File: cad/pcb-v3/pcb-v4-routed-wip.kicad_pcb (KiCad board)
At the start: 4 copper layers, 19.3 x 19.3 mm, 50 parts

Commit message: Zone fill landed; BOM gains U5 + the three 0201s. 4 blockers left.
The KiCad fill worked -- blocker 18 (zones carry no fill) is cleared and
preflight now sees the In2.Cu plane.

NOTE THE FILE FORMAT CHANGED UNDER US. KiCad 20260206 rewrote the board from
(net <n>) + (net_name "X") to a single (net "X"): 165 numbered declarations
and 980 bare ordinals became 0, replaced by 1100 name strings. preflight
survives it (check 4 still matches 134 pins) but any parser in this repo keyed
on (net <digits>) will silently read ZERO nets on a board saved by this KiCad.
Checked before trusting the output rather than after.

BOM: U5 C6989585 (consigned from Digi-Key, JLC stock 0/min 5), R8 C274872,
R9 C273271, C14 C76939 -- the 25 V cap, not the 10 V one, because DC bias
already cost C1/C2 once. Blocker 21 cleared.

Remaining: 4 clearance violations, 16 true open pads, 11 router DRC
violations, GND not fully connected.
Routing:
- net GND: track 0.00 -> 19.9 mm, vias 0 -> 16
- added copper zone on In2.Cu, net GND

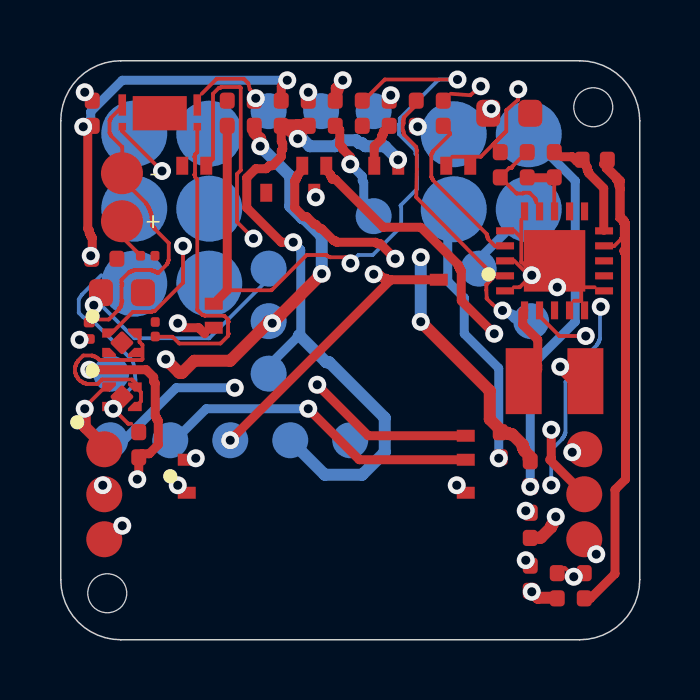
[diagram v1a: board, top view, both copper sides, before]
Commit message: Routing: 3 opens left, and none of them are the PCM's
Placing the 0201s nearest-to-U5 was the wrong objective and it was mine. It
walked R8/R9/C14 up the LEFT STRIP -- 2.72 mm wide, already carrying U3, U4
(X2SON-4, pads 0.34-0.40 apart) and C5 -- and the opens came back clustered on
exactly those parts. They are now scored by ELBOW ROOM within a bounded radius
of U5 instead.

  before: 10-12 open pads pre-stitch, 4 NO PATH after
  after :  4 open pads pre-stitch, 3 NO PATH after

PCM_VDD R8.2 and BL_RETURN R6.1 are gone -- the parts the PCM added now route.

Bounded, not free: pure elbow room threw R9 21.5 mm into the far corner, and
R9 is the V- sense leg, a high-impedance node feeding a comparator that trips
on 20 mV. Distance there is an aerial, not a resistance. SMALL_NEAR caps the
trade. Removing the cluster gate on U5 also mattered: it had dragged U5 itself
from 2.28 to 8.81 mm off the cell pad chasing a target the new objective does
not optimise.

Remaining 3 (VBAT U2.18, VBAT_OK U2.13, VSTOR U4.4) are the U2/U4 knot
ROUTING-RESULT.md named as this board's hard corner before the PCM existed --
0.5 mm-pitch QFN, 0.26 mm pad gaps, ~0.21 mm of escape ring per side. They
resist the router in six configurations and handroute at correct rules.

Also: router and gnd_taps now use 0.45/0.20 vias, JLC's documented standard
floor (preflight check 8) rather than the conservative 0.6/0.3. Taps went
16 -> 21 on the earlier board.
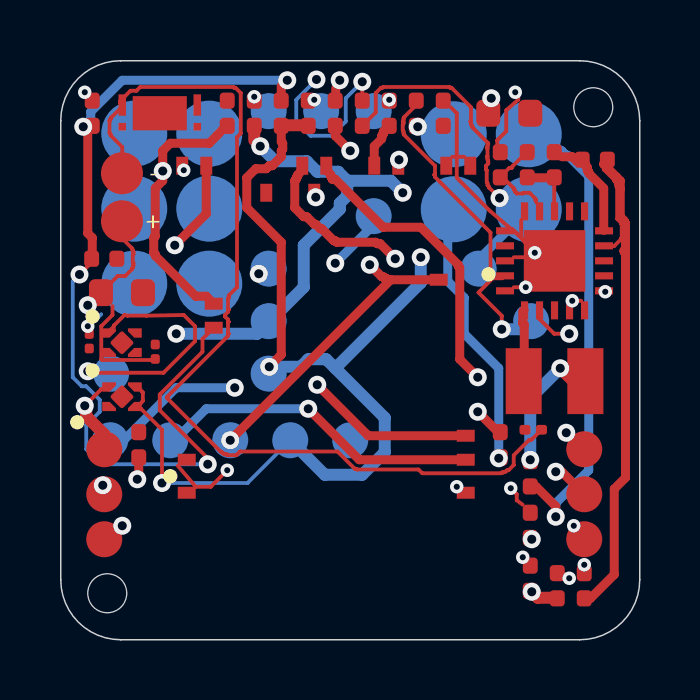
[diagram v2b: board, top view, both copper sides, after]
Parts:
- moved C14 15.2 mm to (6.10, 2.65), turned to 0 degrees
- moved R8 3.21 mm to (-6.50, 0.05), turned to 90 degrees
- moved R9 2.24 mm to (-8.70, -0.30)
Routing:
- net CELL_NEG: track 10.3 -> 32.8 mm
- net SENSOR_3V3: track 44.6 -> 26.6 mm, vias 8 -> 5
- net VBAT_SENSE: track 17.9 -> 30.7 mm
- net PCM_VM: track 10.6 -> 0.00 mm
- net VIN_DC: track 33.9 -> 24.4 mm
- net BL_RETURN: track 2.71 -> 12.2 mm, vias 0 -> 1
- net PCM_VDD: track 9.46 -> 0.00 mm, vias 2 -> 0
- net VREF_SAMP: track 5.24 -> 0.00 mm
- net SENSOR_MCU_3V3: track 20.5 -> 25.4 mm, vias 4 -> 3
- net VBAT: track 9.39 -> 14.1 mm, vias 1 -> 2
- net GND: track 19.9 -> 15.5 mm, vias 16 -> 18
- net HARV_2: track 13.0 -> 16.1 mm
- net BL_FLAG: track 23.0 -> 21.0 mm, vias 2 -> 3
- net SENSOR_TX: track 15.3 -> 14.4 mm
- net RESET: track 18.1 -> 17.5 mm
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
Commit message: Two-stage route: zero-copper nets eliminated, 18 -> 9 true open pads
CORRECTION TO THE PREVIOUS COMMIT. Its '3 opens left' was measured with
stitch_open's NO-PATH count, which only sees pads in nets that have SOME
copper. A net with NO copper at all registers as nothing. PCM_VDD, PCM_VM and
VREF_SAMP had been dropped ENTIRELY -- the router never routed them -- so the
elbow-room placement had traded 'routed but open' for 'not routed', and
preflight check 6 read 18 true open pads (9 of them in zero-copper nets)
against 16 for the placement it replaced. It was a regression, not a win.

Fix: route in two stages. PCM_VDD, PCM_VM, CELL_NEG and VREF_SAMP go FIRST,
alone, before anything can wall them in -- all four succeed -- then everything
else routes with --keep-input-copper around them. 29 of 30 nets now carry
copper; the only empty one is GND, which is the plane's job.

  true open pads   16/18 -> 9,  zero-copper nets 9 -> 0
  clearance (chk 2) BLOCKER -> clear

check_drc's 48 violations were 38 parts measurement error: KiCad 10 keeps
design rules in the .kicad_pro, and none sat beside the board, so check_drc
fell back to a 0.20 default while we route to 0.10. The arithmetic gave it
away -- a via with 0.159 mm of real gap to a J11 pogo pad was reported as
0.041 mm of overlap, which is exactly 1.325 + 0.20 - 1.4841. With the correct
.kicad_pro alongside: 48 -> 10. The .kicad_pro is now committed next to the
board so this cannot recur.
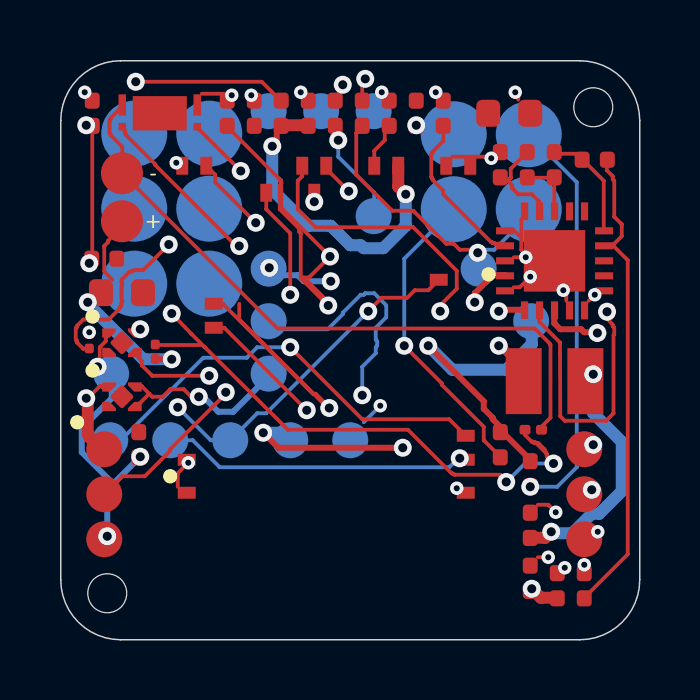
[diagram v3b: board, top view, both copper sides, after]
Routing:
- net PCM_VDD: track 0.00 -> 27.4 mm, vias 0 -> 4
- net SENSOR_MCU_3V3: track 25.4 -> 9.05 mm
- net BL_FLAG: track 21.0 -> 37.2 mm, vias 3 -> 4
- net VBAT: track 14.1 -> 26.4 mm, vias 2 -> 5
- net PCM_VM: track 0.00 -> 11.3 mm, vias 0 -> 2
- net VSTOR: track 56.4 -> 67.1 mm, vias 6 -> 8
- net CELL_NEG: track 32.8 -> 22.2 mm
- net SENSOR_SW_EN: track 0.00 -> 10.5 mm, vias 0 -> 2
- net RESET: track 17.5 -> 26.1 mm
- net GND: track 15.5 -> 8.19 mm, vias 18 -> 22
- net VBAT_OK: track 17.0 -> 10.1 mm, vias 3 -> 2
- net VREF_SAMP: track 0.00 -> 5.26 mm
- net VIN_DC: track 24.4 -> 29.1 mm, vias 5 -> 4
- net SENSOR_3V3: track 26.6 -> 23.0 mm, vias 5 -> 2
- net SENSOR_RX: track 15.4 -> 18.7 mm
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
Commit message: DRC clean: 48 reported violations were 3 bugs and 1 unauthorised change of mine
check_drc now reports NO DRC VIOLATIONS at the project's pinned floor. None of
the 48 were fixed by moving copper; all four causes were in the measuring or
in a rule I changed without saying so.

1. MISSING .kicad_pro (-38). KiCad 10 keeps design rules in the project file,
   and none sat beside the board, so check_drc fell back to a 0.20 default
   while we route to 0.10. The arithmetic gave it away: a via with 0.159 mm of
   real gap to a J11 pogo pad was reported as 0.041 mm of OVERLAP, which is
   exactly 1.325 + 0.20 - 1.4841. The .kicad_pro is now committed beside the
   board.

2. THE ROUTER REWROTE THE DESIGN RULES (-6). min_clearance and
   min_hole_clearance read 0.1187 -- not a number anyone chose, just whatever
   the router achieved, written back as if it were the rule. This is the exact
   behaviour ROUTING-SETTINGS.md warns about ('Fix DRC settings after routing
   -- UNTICKED ... it rewrites your design rules to match whatever the router
   did'). Restored to the 0.10 in fab_floor_touchid.txt.

3. gnd_taps MODELLED THE BOARD AS A SQUARE (-1). The outline has R2.0 corners.
   A via at (-8.85,-8.60) cleared both straight edges (|x| 9.07, |y| 8.82 vs
   9.35) while its copper reached 1.7555 from the arc centre against the 2.0
   radius -- 0.2445 where 0.30 is needed. masks() now tests the corner arcs.

4. stitch_open UNDER-COVERED CUSTOM PADS (-3), and this one it laid itself.
   U3/U4 are TPS7A2033 X2SON-4: their pads are shape 'custom' with a (size) of
   0.1485 mm that is only the ANCHOR, the real outline living in (primitives).
   stitch modelled the anchor and ran track through the actual copper, three
   times into U4.2. gnd_taps had already learned this and grown a
   circumscribed-circle fallback; the fix was never ported. It is now. Note
   stitch honestly reports NO PATH for SENSOR_MCU_3V3 U4.1 afterwards -- that
   connection was never legal, the tool just could n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
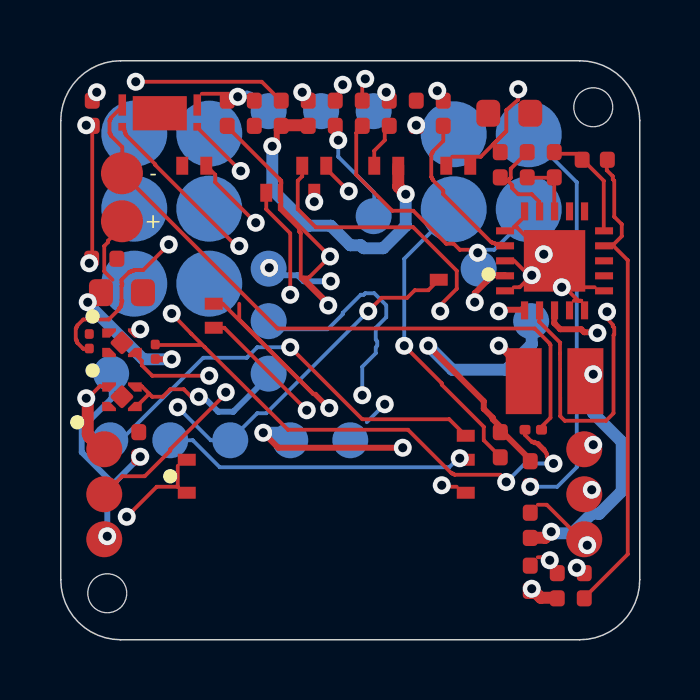
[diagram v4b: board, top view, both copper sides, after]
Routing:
- net GND: track 8.19 -> 17.4 mm, vias 22 -> 15
- net SENSOR_MCU_3V3: track 9.05 -> 7.88 mm, vias 3 -> 2
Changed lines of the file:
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@@
 	)
 	(segment (start -6.3500 -0.1750) (end -5.0000 -0.1750) (width 0.127) (layer "F.Cu") (net 12))
-	(segment (start -8.1250 -0.5000) (end -8.1250 -0.4500) (width 0.127) (layer "F.Cu") (net 16))
-	(segment (start -8.1250 -0.4500) (end -8.1500 -0.4250) (width 0.127) (layer "F.Cu") (net 16))
-	(segment (start -8.1500 -0.4250) (end -8.1500 -0.3000) (width 0.127) (layer "F.Cu") (net 16))
-	(segment (start -8.1500 -0.3000) (end -8.3500 -0.1000) (width 0.127) (layer "F.Cu") (net 16))
-	(segment (start -8.3500 -0.1000) (end -8.3500 0.4750) (width 0.127) (layer "F.Cu") (net 16))
-	(segment (start -8.3500 0.4750) (end -8.4250 0.5500) (width 0.127) (layer "F.Cu") (net 16))
 	(segment (start -8.0000 -3.7250) (end -8.0750 -3.6500) (width 0.127) (layer "F.Cu") (net 23))
 	(segment (start -8.0750 -3.6500) (end -8.0750 -3.6000) (width 0.127) (layer "F.Cu") (net 23))
@@
 	(segment (start -8.2000 -3.4750) (end -8.2000 -2.6250) (width 0.127) (layer "F.Cu") (net 23))
 	(segment (start -8.2000 -2.6250) (end -7.9250 -2.3500) (width 0.127) (layer "F.Cu") (net 23))
-	(via (at -8.4250 0.5500) (size 0.6) (drill 0.3) (layers "F.Cu" "B.Cu") (net 16))
 	(zone
 		(net 4)
@@
 		)
 	)
-	(segment (start 6.2500 5.1500) (end 6.6000 5.1500) (width 0.127) (layer "F.Cu") (net 4))
-	(segment (start 6.6000 5.1500) (end 6.8500 5.4000) (width 0.127) (layer "F.Cu") (net 4))
-	(segment (start 6.2500 6.9000) (end 6.6000 6.9000) (width 0.127) (layer "F.Cu") (net 4))
-	(segment (start 5.6000 -8.3500) (end 5.6000 -8.5000) (width 0.127) (layer "F.Cu") (net 4))
-	(segment (start 5.6000 -8.5000) (end 5.5000 -8.6000) (width 0.127) (layer "F.Cu") (net 4))
-	(segment (start 0.4500 2.4000) (end 1.0000 1.8500) (width 0.127) (layer "B.Cu") (net 4))
-	(segment (start -5.7500 4.5500) (end -5.7500 4.1000) (width 0.127) (layer "F.Cu") (net 4))
-	(segment (start -5.7500 4.1000) (end -5.4000 3.7500) (width 0.127) (layer "F.Cu") (net 4))
-	(segment (start 3.4000 -6.4500) (end 4.5500 -6.4500) (width 0.127) (layer "F.Cu") (net 4))
+	(segment (start 6.2500 5.1500) (end 6.5500 5.1500) (width 0.127) (layer "F.Cu") (net 4))
+	(segment (start 6.5500 5.1500) (end 7.9000 6.5000) (width 0.127) (layer "F.Cu") (net 4))
+	(segment (start 6.2500 6.9000) (end 6.5500 6.9000) (width 0.127) (layer "F.Cu") (net 4))
+	(segment (start 6.5500 6.9000) (end 6.6500 7.0000) (width 0.127) (layer "F.Cu") (net 4))
+	(segment (start -3.8500 -8.5500) (end -3.7500 -8.4500) (width 0.127) (layer "F.Cu") (net 4))
+	(segment (start 5.6000 -8.3500) (end 5.6000 -8.7000) (width 0.127) (layer "F.Cu") (net 4))
+	(segment (start 0.5500 2.4000) (end 1.1500 1.8000) (width 0.127) (layer "B.Cu") (net 4))
+	(segment (start 4.7500 -6.8500) (end 5.2000 -7.3000) (width 0.127) (layer "F.Cu") (net 4))
+	(segment (start 5.2000 -7.3000) (end 5.2000 -8.0000) (width 0.127) (layer "F.Cu") (net 4))
+	(segment (start 5.2000 -8.0000) (end 5.6000 -8.3500) (width 0.127) (layer "F.Cu") (net 4))
+	(segment (start -3.3000 -8.5500) (end -3.4500 -8.6000) (width 0.127) (layer "B.Cu") (net 4))
+	(segment (start -5.7500 4.5500) (end -6.4500 4.5500) (width 0.127) (layer "F.Cu") (net 4))
+	(segment (start -6.4500 4.5500) (end -7.4500 5.5500) (width 0.127) (layer "F.Cu") (net 4))
+	(segment (start -5.7500 3.8500) (end -5.7500 4.5500) (width 0.127) (layer "F.Cu") (net 4))
+	(segment (start 3.4000 -6.4500) (end 4.3500 -6.4500) (width 0.127) (layer "F.Cu") (net 4))
+	(segment (start 4.3500 -6.4500) (end 5.2000 -7.3000) (width 0.127) (layer "F.Cu") (net 4))
+	(segment (start 3.5500 4.5500) (end 3.1000 4.5500) (width 0.127) (layer "F.Cu") (net 4))
 	(segment (start 5.4500 -2.1000) (end 5.6500 -2.1000) (width 0.127) (layer "F.Cu") (net 4))
-	(segment (start 5.6500 -2.1000) (end 6.0000 -2.4500) (width 0.127) (layer "F.Cu") (net 4))
-	(segment (start 7.9500 -1.6500) (end 8.0500 -1.7500) (width 0.127) (layer "F.Cu") (net 4))
-	(segment (start 7.2000 -1.6500) (end 7.2000 -1.9000) (width 0.127) (layer "F.Cu") (net 4))
-	(segment (start 7.2000 -1.9000) (end 7.1000 -2.0000) (width 0.127) (layer "F.Cu") (net 4))
-	(segment (start 5.4500 -3.1000) (end 5.8500 -3.1000) (width 0.127) (layer "F.Cu") (net 4))
-	(segment (start 5.4500 -4.0000) (end 5.7000 -3.7500) (width 0.127) (layer "F.Cu") (net 4))
-	(segment (start 5.7000 -3.7500) (end 5.7000 -3.3500) (width 0.127) (layer "F.Cu") (net 4))
-	(segment (start 5.7000 -3.3500) (end 5.8000 -3.2500) (width 0.127) (layer "F.Cu") (net 4))
-	(segment (start 5.7000 -4.3500) (end 5.7000 -3.7500) (width 0.127) (layer "F.Cu") (net 4))
-	(segment (start -4.9500 -8.5500) (end -4.1000 -8.5500) (width 0.127) (layer "F.Cu") (net 4))
-	(via (at 6.8500 5.4000) (size 0.45) (drill 0.2) (layers "F.Cu" "B.Cu") (net 4))
-	(via (at 6.6000 6.9000) (size 0.45) (drill 0.2) (layers "F.Cu" "B.Cu") (net 4))
-	(via (at -3.9500 -8.5000) (size 0.45) (drill 0.2) (layers "F.Cu" "B.Cu") (net 4))
-	(via (at 7.1500 7.2500) (size 0.45) (drill 0.2) (layers "F.Cu" "B.Cu") (net 4))
-	(via (at -1.6500 -8.6000) (size 0.45) (drill 0.2) (layers "F.Cu" "B.Cu") (net 4))
-	(via (at 2.8500 -8.6000) (size 0.45) (drill 0.2) (layers "F.Cu" "B.Cu") (net 4))
-	(via (at -3.3000 -8.5000) (size 0.45) (drill 0.2) (layers "F.Cu" "B.Cu") (net 4))
-	(via (at 5.5000 -8.6000) (size 0.45) (drill 0.2) (layers "F.Cu" "B.Cu") (net 4))
-	(via (at 1.0500 -8.6000) (size 0.45) (drill 0.2) (layers "F.Cu" "B.Cu") (net 4))
-	(via (at 8.2500 6.0500) (size 0.45) (drill 0.2) (layers "F.Cu" "B.Cu") (net 4))
-	(via (at 1.0000 1.8500) (size 0.45) (drill 0.2) (layers "F.Cu" "B.Cu") (net 4))
-	(via (at -8.8500 -8.6000) (size 0.45) (drill 0.2) (layers "F.Cu" "B.Cu") (net 4))
-	(via (at -8.7000 -0.6000) (size 0.45) (drill 0.2) (layers "F.Cu" "B.Cu") (net 4))
-	(via (at 7.8000 7.1500) (size 0.45) (drill 0.2) (layers "F.Cu" "B.Cu") (net 4))
-	(via (at 4.7000 -6.4000) (size 0.45) (drill 0.2) (layers "F.Cu" "B.Cu") (net 4))
-	(via (at -5.4000 3.7500) (size 0.45) (drill 0.2) (layers "F.Cu" "B.Cu") (net 4))
-	(via (at -5.8000 -6.2500) (size 0.45) (drill 0.2) (layers "F.Cu" "B.Cu") (net 4))
-	(via (at 3.5500 4.6000) (size 0.45) (drill 0.2) (layers "F.Cu" "B.Cu") (net 4))
-	(via (at 6.0000 -2.4500) (size 0.45) (drill 0.2) (layers "F.Cu" "B.Cu") (net 4))
-	(via (at 8.1500 -1.8500) (size 0.45) (drill 0.2) (layers "F.Cu" "B.Cu") (net 4))
-	(via (at 7.1000 -2.0000) (size 0.45) (drill 0.2) (layers "F.Cu" "B.Cu") (net 4))
-	(via (at 5.8500 -3.1000) (size 0.45) (drill 0.2) (layers "F.Cu" "B.Cu") (net 4))
+	(segment (start 5.6500 -2.1000) (end 6.0500 -2.5000) (width 0.127) (layer "F.Cu") (net 4))
+	(segment (start 8.1500 -2.1000) (end 7.0500 -2.1000) (width 0.127) (layer "F.Cu") (net 4))
+	(segment (start 7.7000 -1.6500) (end 7.6000 -1.6500) (width 0.127) (layer "F.Cu") (net 4))
+	(segment (start 7.6000 -1.6500) (end 7.2500 -2.0000) (width 0.127) (layer "F.Cu") (net 4))
+	(segment (start 7.4500 -1.6500) (end 7.7000 -1.6500) (width 0.127) (layer "F.Cu") (net 4))
+	(segment (start 5.4500 -3.0000) (end 5.8500 -2.6000) (width 0.127) (layer "F.Cu") (net 4))
+	(segment (start 5.4500 -4.1000) (end 5.5500 -4.1000) (width 0.127) (layer "F.Cu") (net 4))
+	(segment (start 5.5500 -4.1000) (end 6.4500 -3.2000) (width 0.127) (layer "F.Cu") (net 4))
+	(segment (start 5.7000 -4.3500) (end 5.4500 -4.1000) (width 0.127) (layer "F.Cu") (net 4))
+	(segment (start -4.9500 -8.5500) (end -3.9500 -8.5500) (width 0.127) (layer "F.Cu") (net 4))
+	(via (at 7.9000 6.5000) (size 0.6) (drill 0.3) (layers "F.Cu" "B.Cu") (net 4))
+	(via (at 6.6500 7.0000) (size 0.6) (drill 0.3) (layers "F.Cu" "B.Cu") (net 4))
+	(via (at -3.7500 -8.4500) (size 0.6) (drill 0.3) (layers "F.Cu" "B.Cu") (net 4))
+	(via (at -1.6000 -8.6000) (size 0.6) (drill 0.3) (layers "F.Cu" "B.Cu") (net 4))
+	(via (at 2.9000 -8.6500) (size 0.6) (drill 0.3) (layers "F.Cu" "B.Cu") (net 4))
+	(via (at 5.6000 -8.7000) (size 0.6) (drill 0.3) (layers "F.Cu" "B.Cu") (net 4))
+	(via (at 1.2000 -8.6000) (size 0.6) (drill 0.3) (layers "F.Cu" "B.Cu") (net 4))
+	(via (at 1.1500 1.8000) (size 0.6) (drill 0.3) (layers "F.Cu" "B.Cu") (net 4))
+	(via (at -8.4500 -8.6000) (size 0.6) (drill 0.3) (layers "F.Cu" "B.Cu") (net 4))
+	(via (at 7.5500 7.2500) (size 0.6) (drill 0.3) (layers "F.Cu" "B.Cu") (net 4))
+	(via (at -7.4500 5.5500) (size 0.6) (drill 0.3) (layers "F.Cu" "B.Cu") (net 4))
+	(via (at 3.0500 4.5000) (size 0.6) (drill 0.3) (layers "F.Cu" "B.Cu") (net 4))
+	(via (at 6.0500 -2.5000) (size 0.6) (drill 0.3) (layers "F.Cu" "B.Cu") (net 4))
+	(via (at 7.0500 -2.1000) (size 0.6) (drill 0.3) (layers "F.Cu" "B.Cu") (net 4))
+	(via (at 6.4500 -3.2000) (size 0.6) (drill 0.3) (layers "F.Cu" "B.Cu") (net 4))
 )
